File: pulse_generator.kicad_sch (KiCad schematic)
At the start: 18 parts, among them J1 Power, J2 Digital/PWM, J3 Analog, J4 Digital/PWM, J5 Conn_Coaxial, J6 Conn_Coaxial

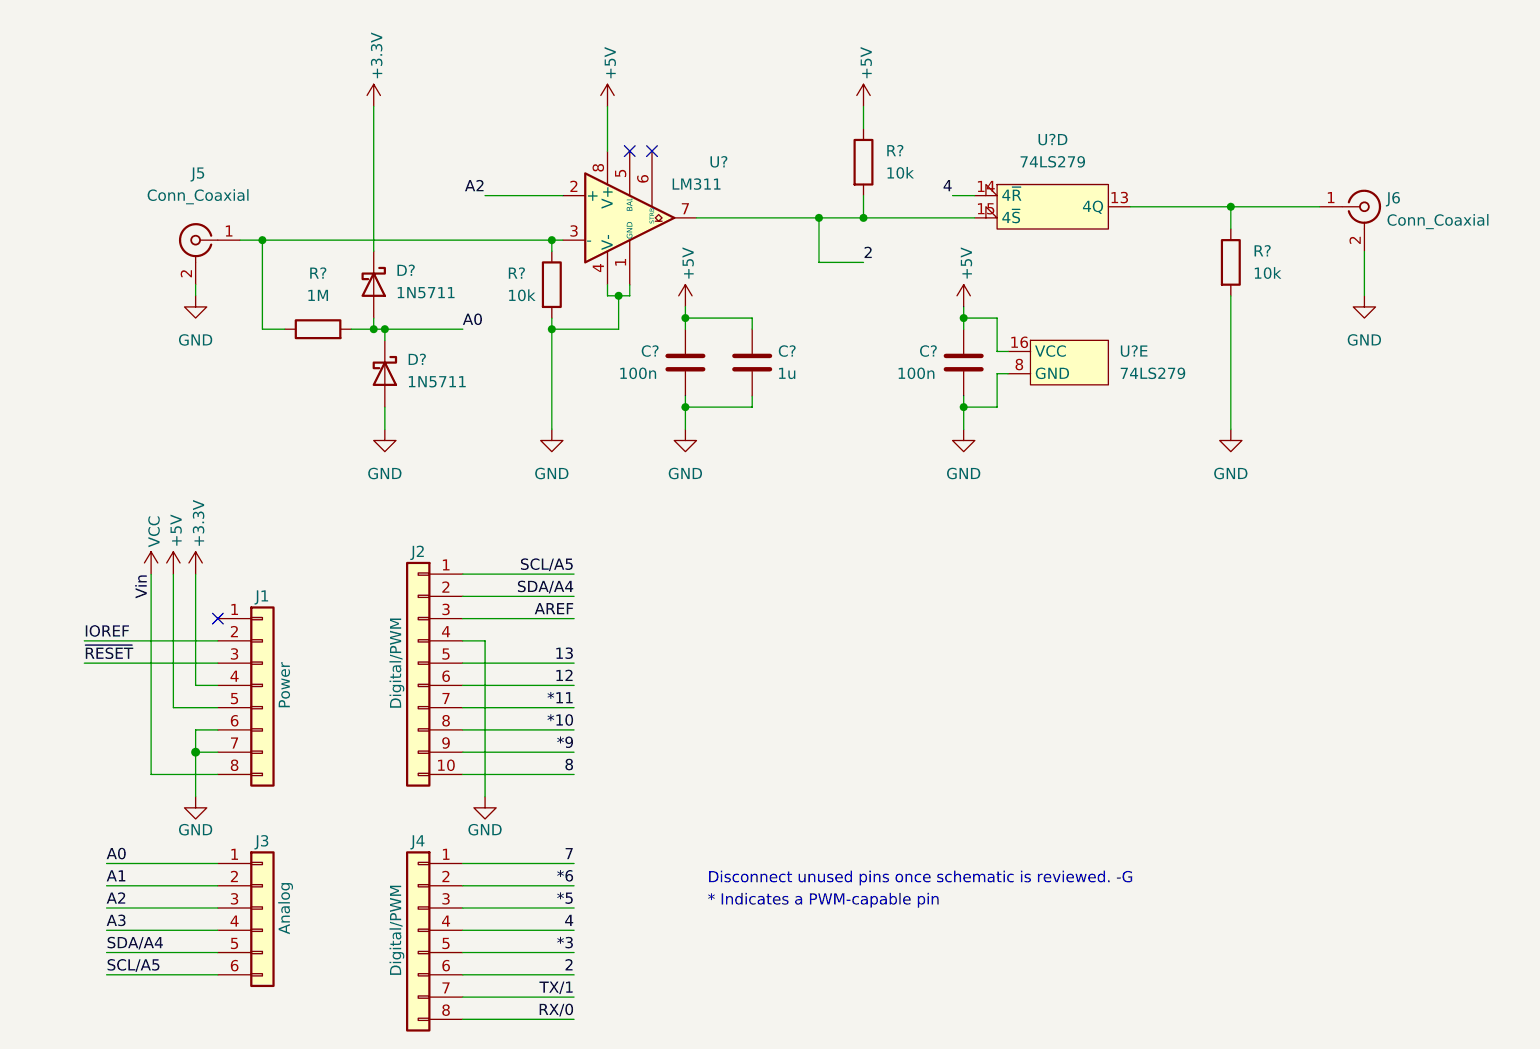
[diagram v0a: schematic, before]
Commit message: decoupling lm311 update
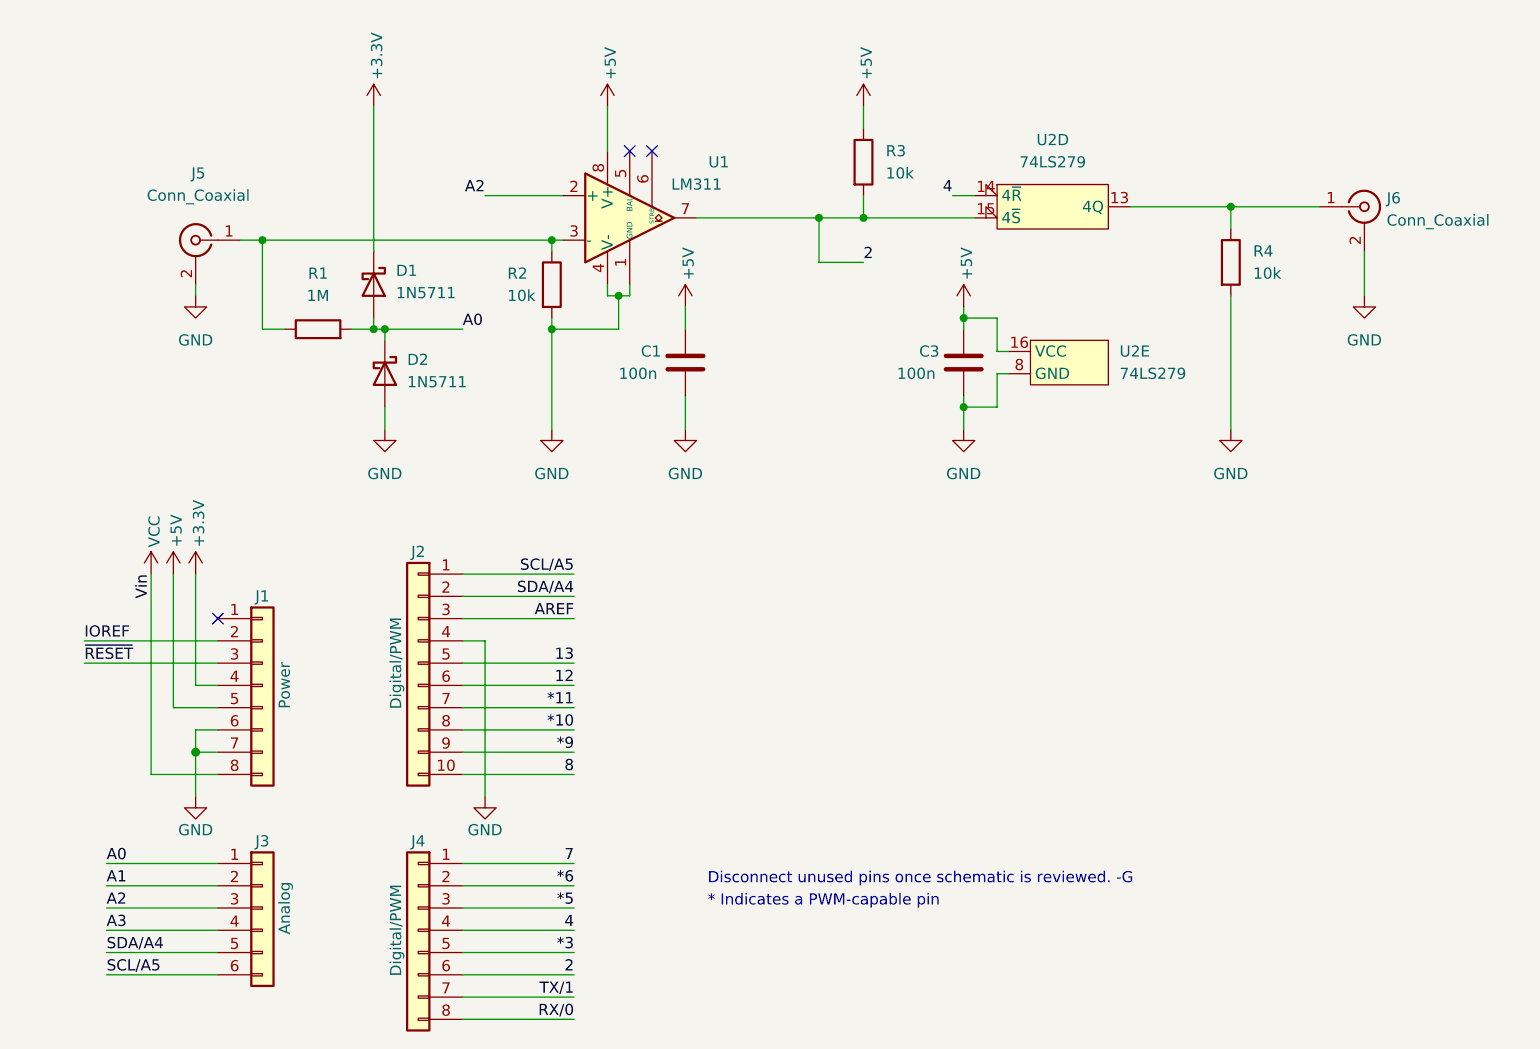
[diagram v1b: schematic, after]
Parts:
- removed C?: 1u, symbol Device:C
- gave numbers to parts that had none: 10
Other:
- title: (none) -> Laser ablator feedback control

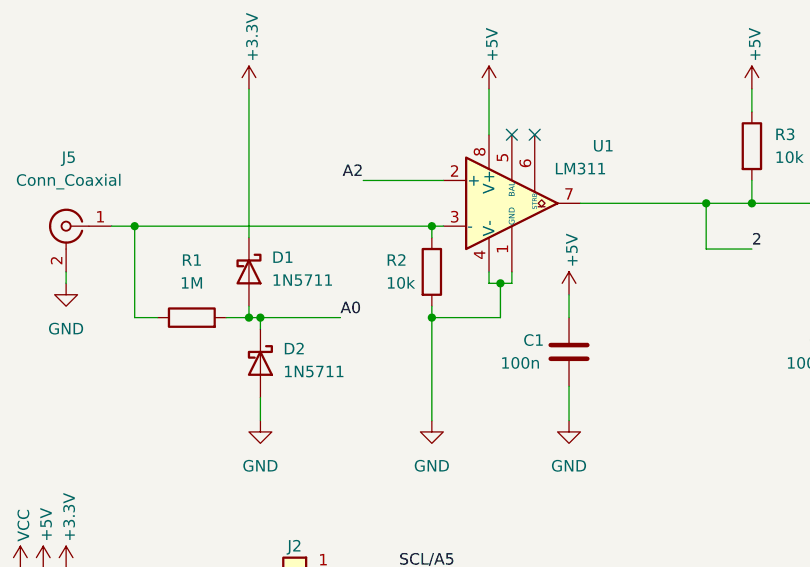
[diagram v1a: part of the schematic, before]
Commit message: wrong comp pd value
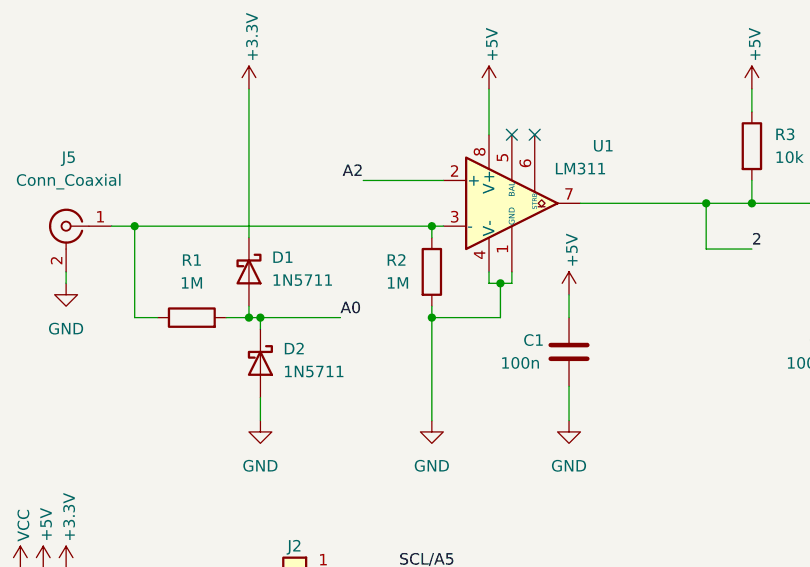
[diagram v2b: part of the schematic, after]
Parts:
- R2: value 10k -> 1M
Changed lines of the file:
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@@
       (effects (font (size 1.27 1.27)) (justify left))
     )
-    (property "Value" "10k" (id 1) (at 69.85 48.26 0)
+    (property "Value" "1M" (id 1) (at 69.85 48.26 0)
       (effects (font (size 1.27 1.27)) (justify left))
     )
@@
     )
     (path "/dff44cf7-f027-4684-a0fc-c5d5d4bc5ca7"
-      (reference "R2") (unit 1) (value "10k") (footprint "")
+      (reference "R2") (unit 1) (value "1M") (footprint "")
     )
     (path "/e6a737eb-f45e-4592-82b9-f475a9872da7"

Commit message: sch rev2
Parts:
- added D3: LED, LED_THT:LED_D5.0mm, symbol Device:LED
- C1, C3: footprint (none) -> Capacitor_SMD:C_0805_2012Metric_Pad1.18x1.45mm_HandSolder
- D1, D2: footprint (none) -> Diode_SMD:D_SOD-123
- R1, R2, R3: footprint (none) -> Resistor_SMD:R_0805_2012Metric_Pad1.20x1.40mm_HandSolder
- R4: value 10k -> 330; footprint (none) -> Resistor_SMD:R_0805_2012Metric_Pad1.20x1.40mm_HandSolder
- U1: footprint (none) -> Package_DIP:DIP-8_W7.62mm_LongPads
- U2: footprint (none) -> Package_DIP:DIP-16_W7.62mm_LongPads
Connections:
- net GND: now also D3.1 (K); no longer R4.2
- net SCL/A5: no longer names the net of J2.1 (Pin_1)
- net SCL/A5: no longer J3.6 (Pin_6)
- net SDA/A4: no longer names the net of J2.2 (Pin_2)
- net SDA/A4: no longer J3.5 (Pin_5)
- new net: D3.2 (A), R4.2
- no-connect marks 3 -> 7
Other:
- moved on the sheet: D1, D2, R1, R2

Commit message: nucleo form factor
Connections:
- net A0: now also U1.2 (+); no longer D1.2 (A), D2.1 (K), R1.2
- net A2: now also D1.2 (A), D2.1 (K), R1.2; no longer U1.2 (+)
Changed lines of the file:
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@@
   (junction (at 105.41 39.37) (diameter 0) (color 0 0 0 0)
   )
+  (junction (at 110.49 39.37) (diameter 0) (color 0 0 0 0)
+  )
+  (junction (at 121.92 50.8) (diameter 0) (color 0 0 0 0)
+  )
+  (junction (at 152.4 38.1) (diameter 0) (color 0 0 0 0)
+  )
   (junction (at 64.77 52.07) (diameter 0) (color 0 0 0 0)
-  )
-  (junction (at 110.49 39.37) (diameter 0) (color 0 0 0 0)
-  )
-  (junction (at 121.92 50.8) (diameter 0) (color 0 0 0 0)
-  )
-  (junction (at 152.4 38.1) (diameter 0) (color 0 0 0 0)
   )
   (no_connect (at 64.77 82.55))
@@
     (stroke (width 0) (type default) (color 0 0 0 0))
   )
-  (wire (pts (xy 64.77 52.07) (xy 73.66 52.07))
-    (stroke (width 0) (type default) (color 0 0 0 0))
-  )
   (wire (pts (xy 64.77 100.33) (xy 77.47 100.33))
     (stroke (width 0) (type solid) (color 0 0 0 0))
@@
     (stroke (width 0) (type default) (color 0 0 0 0))
   )
+  (wire (pts (xy 64.77 52.07) (xy 71.12 52.07))
+    (stroke (width 0) (type default) (color 0 0 0 0))
+  )
   (wire (pts (xy 60.96 52.07) (xy 63.5 52.07))
     (stroke (width 0) (type default) (color 0 0 0 0))
@@
     (stroke (width 0) (type default) (color 0 0 0 0))
   )
+  (wire (pts (xy 69.85 36.83) (xy 76.2 36.83))
+    (stroke (width 0) (type default) (color 0 0 0 0))
+  )
   (wire (pts (xy 64.77 53.34) (xy 64.77 52.07))
-    (stroke (width 0) (type default) (color 0 0 0 0))
-  )
-  (wire (pts (xy 67.31 36.83) (xy 76.2 36.83))
     (stroke (width 0) (type default) (color 0 0 0 0))
   )
@@
     (effects (font (size 1.27 1.27)) (justify right bottom))
   )
-  (label "A2" (at 67.31 36.83 180)
-    (effects (font (size 1.27 1.27)) (justify right bottom))
+  (label "A2" (at 71.12 52.07 0)
+    (effects (font (size 1.27 1.27)) (justify left bottom))
   )
   (label "4" (at 120.65 36.83 180)
     (effects (font (size 1.27 1.27)) (justify right bottom))
   )
-  (label "A0" (at 73.66 52.07 0)
-    (effects (font (size 1.27 1.27)) (justify left bottom))
+  (label "A0" (at 69.85 36.83 180)
+    (effects (font (size 1.27 1.27)) (justify right bottom))
   )
   (label "7" (at 77.47 113.03 180)

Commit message: Ready for review
Ready for review
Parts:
- added D4, D5: LED, LED_SMD:LED_0805_2012Metric_Pad1.15x1.40mm_HandSolder, symbol Device:LED
- added R5: 10k, Resistor_SMD:R_0805_2012Metric_Pad1.20x1.40mm_HandSolder, symbol Device:R
- added R6, R7: 330, Resistor_SMD:R_0805_2012Metric_Pad1.20x1.40mm_HandSolder, symbol Device:R
- added SW1: SW_Push, Button_Switch_THT:SW_Tactile_SPST_Angled_PTS645Vx39-2LFS, symbol Switch:SW_Push
- added TP1: GND_hook, Connector_PinHeader_2.54mm:PinHeader_1x01_P2.54mm_Vertical, symbol Connector:TestPoint
- added TP2: DAC_cal, Connector_PinHeader_2.54mm:PinHeader_1x01_P2.54mm_Vertical, symbol Connector:TestPoint
- J1, J4: footprint Connector_PinSocket_2.54mm:PinSocket_1x08_P2.54mm_Vertical -> Connector_PinHeader_2.54mm:PinHeader_1x08_P2.54mm_Vertical
- J2: footprint Connector_PinSocket_2.54mm:PinSocket_1x10_P2.54mm_Vertical -> Connector_PinHeader_2.54mm:PinHeader_1x10_P2.54mm_Vertical
- J3: footprint Connector_PinSocket_2.54mm:PinSocket_1x06_P2.54mm_Vertical -> Connector_PinHeader_2.54mm:PinHeader_1x06_P2.54mm_Vertical
- U1: footprint Package_DIP:DIP-8_W7.62mm_LongPads -> Package_DIP:DIP-8_W7.62mm_Socket_LongPads
- U2: footprint Package_DIP:DIP-16_W7.62mm_LongPads -> Package_DIP:DIP-16_W7.62mm_Socket_LongPads
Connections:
- net +5V: now also D4.2 (A), D5.2 (A)
- net 2: now also R5.1
- net A0: now also TP2.1
- net GND: now also R5.2, R6.1, R7.2, SW1.1, TP1.1
- net ~{RESET}: now also SW1.2
- new net: D4.1 (K), R7.1
- new net: D5.1 (K), R6.2
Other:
- note removed: "Disconnect unused pins once schematic is reviewed. -G"
- title: Laser ablator feedback control -> Pulsed laser ablator PLL Interface

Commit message: corrected some stuff, larger enclosure
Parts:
- added R8, R9: 0, Resistor_SMD:R_0805_2012Metric_Pad1.20x1.40mm_HandSolder, symbol Device:R
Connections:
- net GND: now also R8.2, R9.2; no longer J5.2 (Ext), J6.2 (Ext)
- new net: J5.2 (Ext), R8.1
- new net: J6.2 (Ext), R9.1
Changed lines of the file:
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@@
   (junction (at 73.66 36.83) (diameter 0) (color 0 0 0 0)
+  )
+  (junction (at 44.45 57.15) (diameter 0) (color 0 0 0 0)
   )
   (junction (at 110.49 39.37) (diameter 0) (color 0 0 0 0)
@@
     (stroke (width 0) (type solid))
   )
+  (wire (pts (xy 167.64 55.88) (xy 167.64 63.5))
+    (stroke (width 0) (type default))
+  )
   (wire (pts (xy 31.75 80.01) (xy 31.75 95.25))
     (stroke (width 0) (type solid))
@@
     (stroke (width 0) (type solid))
   )
-  (wire (pts (xy 44.45 50.8) (xy 44.45 63.5))
+  (wire (pts (xy 44.45 50.8) (xy 44.45 57.15))
     (stroke (width 0) (type default))
   )
@@
     (stroke (width 0) (type default))
   )
+  (wire (pts (xy 34.29 57.15) (xy 44.45 57.15))
+    (stroke (width 0) (type default))
+  )
   (wire (pts (xy 64.77 100.33) (xy 77.47 100.33))
     (stroke (width 0) (type solid))
   )
+  (wire (pts (xy 34.29 55.88) (xy 34.29 57.15))
+    (stroke (width 0) (type default))
+  )
   (wire (pts (xy 142.24 92.71) (xy 142.24 93.98))
     (stroke (width 0) (type default))
@@
   (wire (pts (xy 24.13 115.57) (xy 36.83 115.57))
     (stroke (width 0) (type solid))
+  )
+  (wire (pts (xy 44.45 57.15) (xy 44.45 63.5))
+    (stroke (width 0) (type default))
   )
   (wire (pts (xy 152.4 38.1) (xy 162.56 38.1))
@@
     )
   )
-  (symbol (lib_id "power:GND") (at 167.64 48.26 0) (unit 1)
-    (in_bom yes) (on_board yes) (dnp no)
-    (property "Reference" "#PWR017" (at 167.64 54.61 0)
-      (effects (font (size 1.27 1.27)) hide)
-    )
-    (property "Value" "GND" (at 167.64 53.34 0)
-      (effects (font (size 1.27 1.27)))
-    )
-    (property "Footprint" "" (at 167.64 48.26 0)
-      (effects (font (size 1.27 1.27)) hide)
-    )
-    (property "Datasheet" "" (at 167.64 48.26 0)
+  (symbol (lib_id "power:GND") (at 167.64 63.5 0) (unit 1)
+    (in_bom yes) (on_board yes) (dnp no)
+    (property "Reference" "#PWR017" (at 167.64 69.85 0)
+      (effects (font (size 1.27 1.27)) hide)
+    )
+    (property "Value" "GND" (at 167.64 68.58 0)
+      (effects (font (size 1.27 1.27)))
+    )
+    (property "Footprint" "" (at 167.64 63.5 0)
+      (effects (font (size 1.27 1.27)) hide)
+    )
+    (property "Datasheet" "" (at 167.64 63.5 0)
       (effects (font (size 1.27 1.27)) hide)
     )
@@
     )
   )
+  (symbol (lib_id "Device:R") (at 34.29 52.07 0) (unit 1)
+    (in_bom yes) (on_board yes) (dnp no)
+    (property "Reference" "R8" (at 29.21 50.8 0)
+      (effects (font (size 1.27 1.27)) (justify left))
+    )
+    (property "Value" "0" (at 29.21 53.34 0)
+      (effects (font (size 1.27 1.27)) (justify left))
+    )
+    (property "Footprint" "Resistor_SMD:R_0805_2012Metric_Pad1.20x1.40mm_HandSolder" (at 32.512 52.07 90)
+      (effects (font (size 1.27 1.27)) hide)
+    )
+    (property "Datasheet" "~" (at 34.29 52.07 0)
+      (effects (font (size 1.27 1.27)) hide)
+    )
+    (pin "1")
+    (pin "2")
+    (instances
+      (project "pulse_generator"
+        (path "/e63e39d7-6ac0-4ffd-8aa3-1841a4541b55"
+          (reference "R8") (unit 1)
+        )
+      )
+    )
+  )
   (symbol (lib_id "Device:D_Schottky") (at 64.77 57.15 270) (unit 1)
     (in_bom yes) (on_board yes) (dnp no) (fields_autoplaced)
@@
         (path "/e63e39d7-6ac0-4ffd-8aa3-1841a4541b55"
           (reference "D2") (unit 1)
+        )
+      )
+    )
+  )
+  (symbol (lib_id "Device:R") (at 167.64 52.07 0) (unit 1)
+    (in_bom yes) (on_board yes) (dnp no) (fields_autoplaced)
+    (property "Reference" "R9" (at 170.18 51.435 0)
+      (effects (font (size 1.27 1.27)) (justify left))
+    )
+    (property "Value" "0" (at 170.18 53.975 0)
+      (effects (font (size 1.27 1.27)) (justify left))
+    )
+    (property "Footprint" "Resistor_SMD:R_0805_2012Metric_Pad1.20x1.40mm_HandSolder" (at 165.862 52.07 90)
+      (effects (font (size 1.27 1.27)) hide)
+    )
+    (property "Datasheet" "~" (at 167.64 52.07 0)
+      (effects (font (size 1.27 1.27)) hide)
+    )
+    (pin "1")
+    (pin "2")
+    (instances
+      (project "pulse_generator"
+        (path "/e63e39d7-6ac0-4ffd-8aa3-1841a4541b55"
+          (reference "R9") (unit 1)
         )
       )
@@
         )
       )
-    )
-  )
-  (symbol (lib_id "power:GND") (at 34.29 48.26 0) (unit 1)
-    (in_bom yes) (on_board yes) (dnp no) (fields_autoplaced)
-    (property "Reference" "#PWR06" (at 34.29 54.61 0)
-      (effects (font (size 1.27 1.27)) hide)
-    )
-    (property "Value" "GND" (at 34.29 53.34 0)
-      (effects (font (size 1.27 1.27)))
-    )
-    (property "Footprint" "" (at 34.29 48.26 0)
-      (effects (font (size 1.27 1.27)) hide)
-    )
-    (property "Datasheet" "" (at 34.29 48.26 0)
-      (effects (font (size 1.27 1.27)) hide)
-    )
-    (pin "1")
-    (instances
-      (project "pulse_generator"
-        (path "/e63e39d7-6ac0-4ffd-8aa3-1841a4541b55"
-          (reference "#PWR06") (unit 1)
-        )
-      )
